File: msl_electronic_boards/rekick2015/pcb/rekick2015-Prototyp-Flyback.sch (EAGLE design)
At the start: 193 parts, among them IC1 LM1458D, IC2 4043D, IC3 LM1117, IC4 LM1458D, Q1 16MHz, Q2 IGW60T120, Q3 IPP023N10N5, Q5 IPD90P04P4L, Q6 IRF840, T2 BC849, T3 BC849, T4 BC849, T5 IRLML6344TRPBF, T6 BC859, U1 TXB0108PWR, U2 SN74LVC2G02DCTR, U3 LM2675, U4 LM2675

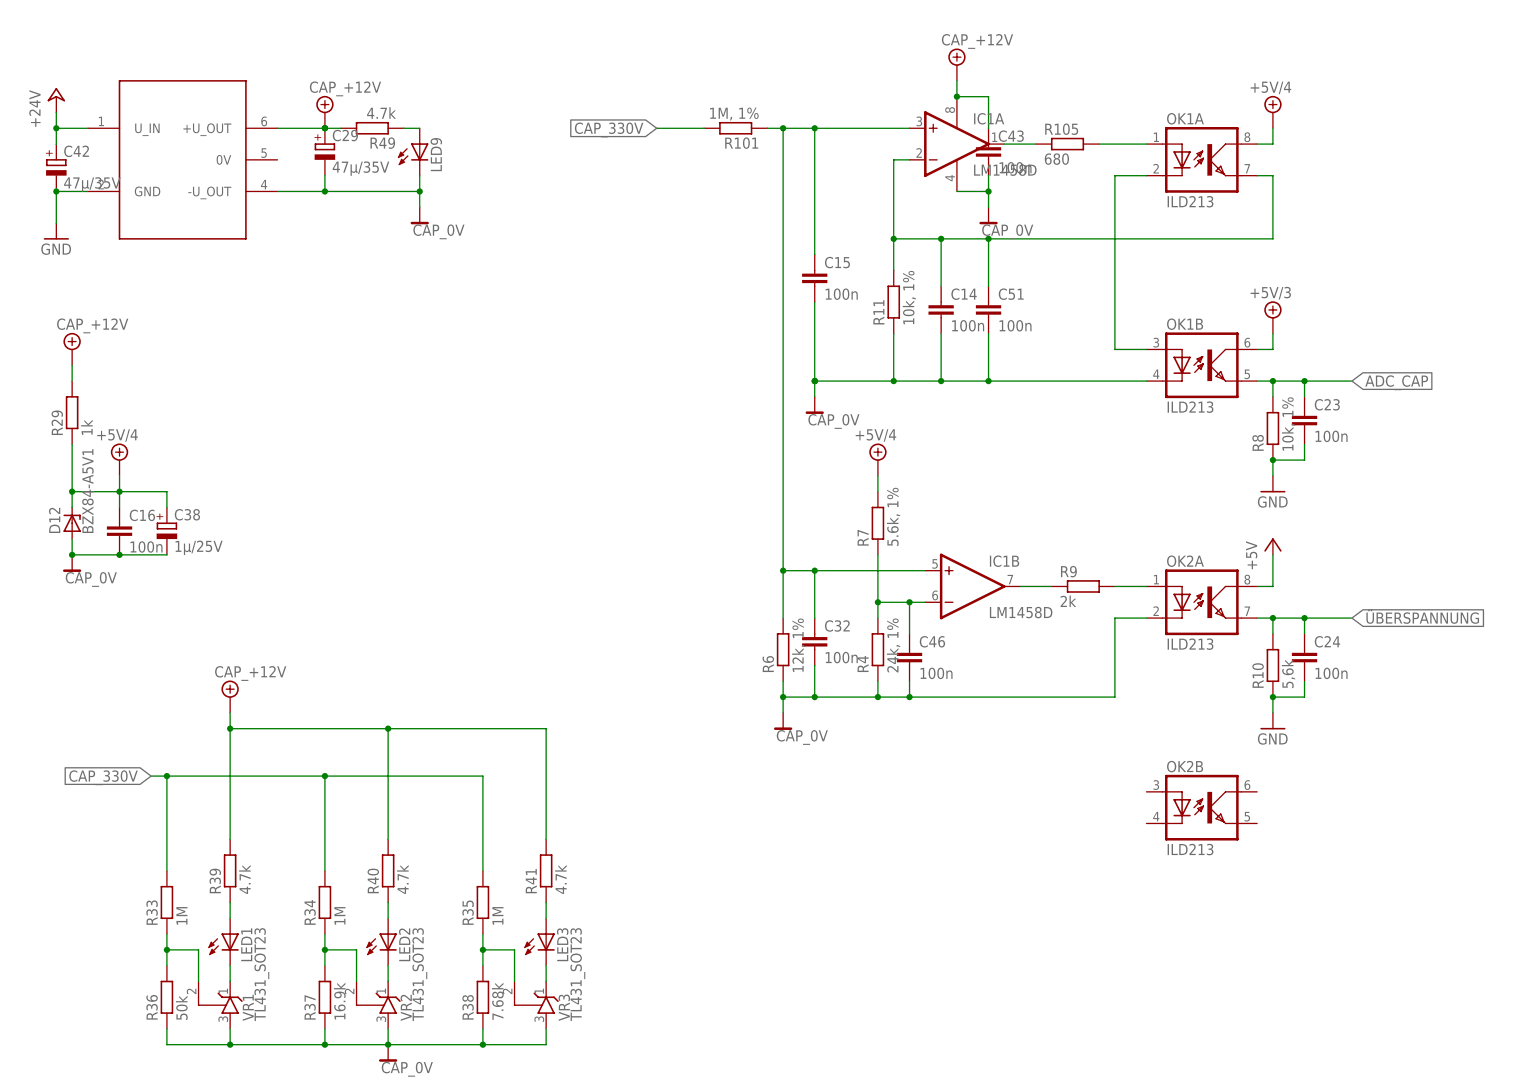
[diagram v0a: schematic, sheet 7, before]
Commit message: rekick flyback
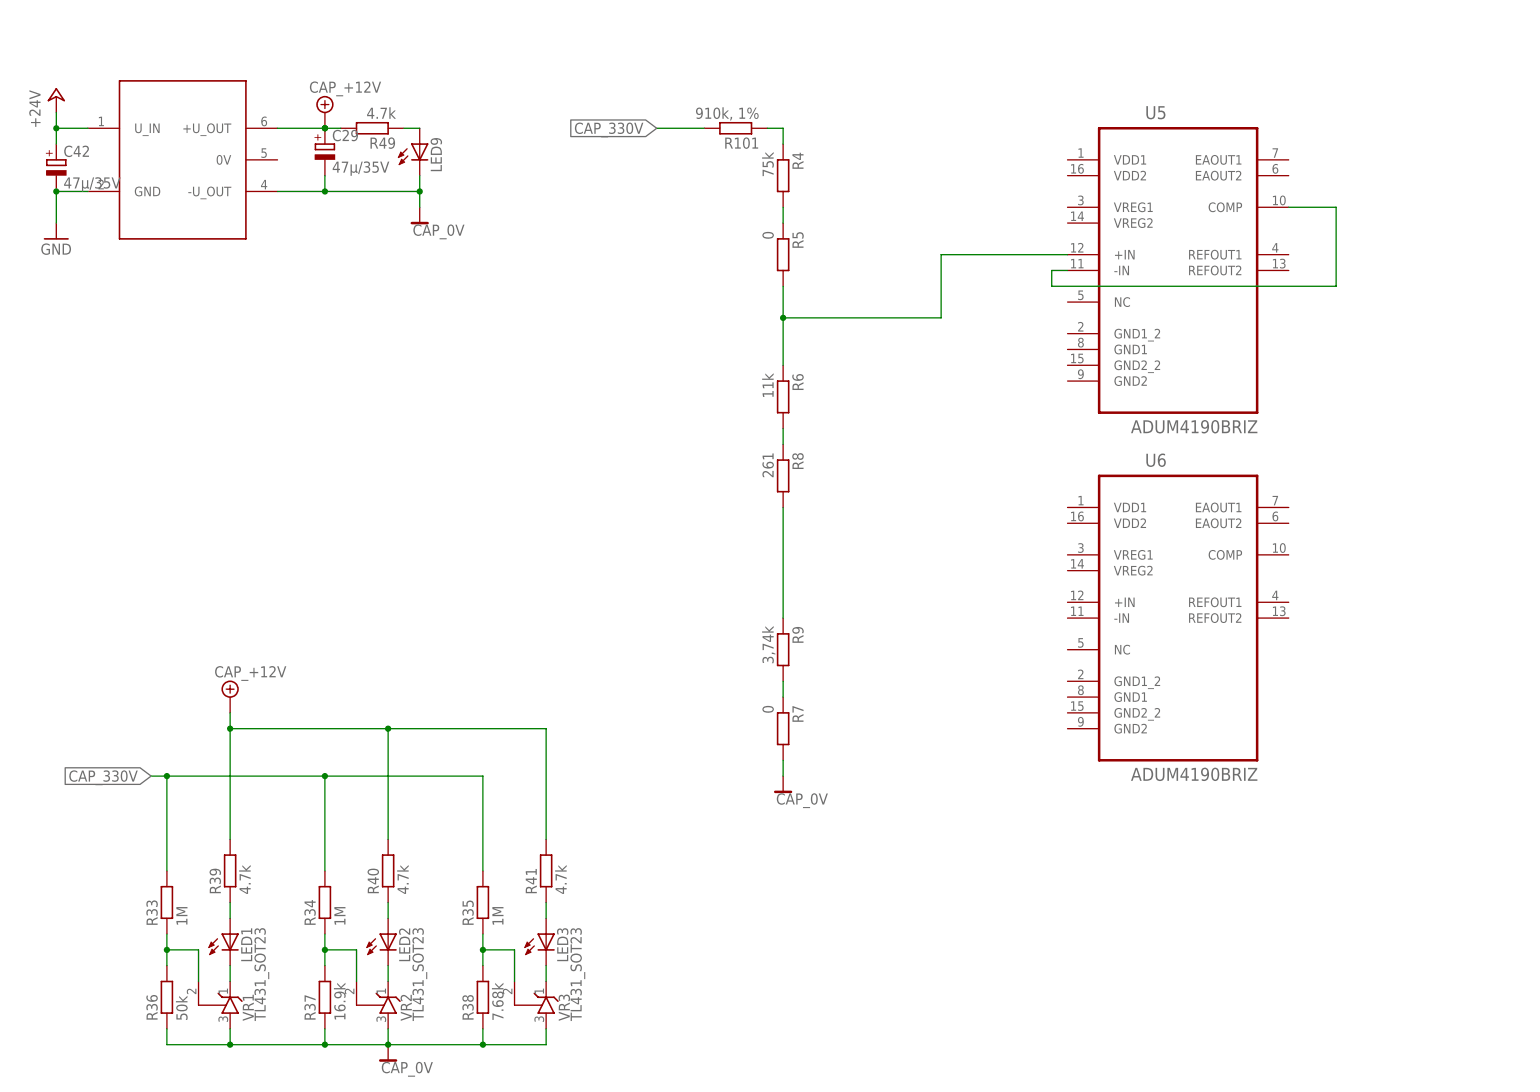
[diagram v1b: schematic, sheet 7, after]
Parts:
- removed C14, C15, C16, C23, C24, C32, C36, C43, C44, C46, C47, C51: 100n, rcl:C-EUC0603
- removed C38: 1µ/25V, rcl:CPOL-EUSMCA
- removed D12: BZX84-A5V1, diode:BZX84CSMD
- removed IC1, IC4: LM1458D, linear:LM1458D
- removed OK1, OK2: ILD213, optocoupler:ILD213
- removed R105: 680, rcl:R-EU_R0805
- removed R12: 10k, rcl:R-EU_R0805
- removed R21: 33k, 1%, rcl:R-EU_R0805
- removed R25: 100k, rcl:R-EU_R0805
- removed R26: 50k, rcl:R-EU_R0805
- removed R29: 1k, rcl:R-EU_R0805
- removed R52: 5,6k, 1%, rcl:R-EU_R0805
- removed T6: BC859, transistor:BC858C-PNP-SOT23-BEC
- added D3: SMD ZD 12, diode:BZX84CSMD
- added R68: 150k, rcl:R-EU_R0805
- added R69, R70, R71: 50k, rcl:R-EU_R0805
- added T1, T7: BC859, transistor:BC858C-PNP-SOT23-BEC
- added U5, U6: ADUM4190BRIZ, adum4190:ADUM4190BRIZ
- R10: value 5,6k -> 910k, 1%; device rcl:R-EU_R0805 -> rcl:R-EU_R2512
- R101: value 1M, 1% -> 910k, 1%
- R11: value 10k, 1% -> 100k
- R13, R18, R66: value 5 -> 4.7
- R4: value 24k, 1% -> 75k
- R48: value 375k -> 220k
- R5: value 10k, 1% -> 0
- R53: value 575k -> 560k
- R54: value 135k -> 130k
- R56: value 375k -> 360k
- R6: value 12k, 1% -> 11k
- R60: value 732 -> 0
- R67: value 375k -> 40.2k
- R7: value 5.6k, 1% -> 0
- R8: value 10k, 1% -> 261
- R9: value 2k -> 3,74k
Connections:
- net N$68 renamed FB
- removed net +5V/4: C16.1, C38.+, D12.C, OK1A.COL, R29.1, R7.2
- removed net CHARGE: U$9.CHARGE
- removed net KICK_VOLTAGE: C36.1, IC4A.-IN, R21.2, R5.1, R52.2
- removed net N$35: OK2A.A, R9.2
- removed net N$50: IC4A.OUT, U2.2B
- removed net N$52: R25.2, T4.B
- removed net N$58: R26.1, T4.C, U2.2A
- new net 0V: R7.2
- new net N$78: R48.1, R68.2, T7.E
- new net N$79: R71.1, T7.B
- new net N$80: R69.1, T1.E, U$9.CHARGE
- new net N$81: R70.1, T1.B
- net +5V: no longer C44.1, IC4P.V+, OK2A.COL, R26.2
- net +5V/3: no longer OK1B.COL, R5.2
- net ACTIVATE_BOOSTER: now also R69.2; no longer R25.1
- net ADC_CAP: no longer C23.1, C47.1, IC4A.+IN, OK1B.EMIT, R8.2
- net CAP_+12V: no longer C43.1, IC1P.V+, R29.2, T6.E
- net CAP_0V: now also D3.A, T4.E; no longer C14.2, C15.2, C16.2, C32.2, C38.-, C43.2, C46.2, C51.2, D12.A, IC1P.V-, OK1B.C, OK2A.C, R12.1, R4.1, R6.1
- net CAP_330V: now also R10.1
- net D2A: no longer R52.1
- net GND: now also T1.C, T7.C; no longer C23.2, C24.2, C36.2, C44.2, C47.2, IC4B.+IN, IC4B.-IN, IC4P.V-, R10.1, R21.1, R8.1, T4.E
- net N$13: now also R7.1, R9.2; no longer IC1A.OUT, R105.1
- net N$14: now also R5.2, R6.1, U5.+IN; no longer C14.1, C51.1, IC1A.-IN, OK1A.EMIT, R11.2
- net N$15: now also R4.2, R5.1; no longer C15.1, C32.1, IC1A.+IN, IC1B.+IN, R101.1, R6.2
- net N$21: now also R101.1, R4.1; no longer OK1A.A, R105.2
- net N$22: now also U5.-IN, U5.COMP; no longer OK1A.C, OK1B.A
- net N$25: now also R8.2; no longer IC1B.OUT
- net N$27: now also R6.2, R8.1; no longer C46.1, IC1B.-IN, R4.2, R7.1
- net N$34: now also R68.1; no longer R48.1
- net N$39: now also D3.C, R10.2, T4.C; no longer R12.2, T6.C
- net N$46: now also R11.2, T4.B; no longer T6.B
- net NOTAUS: now also R70.2, R71.2
- net ÜBERSPANNUNG: no longer C24.1, OK2A.EMIT, R10.2
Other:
- moved on the sheet: C30, R14, R15, R4, R48, R53, R54, R56, R6, R64, R65, R7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

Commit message: rekick flyback
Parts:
- removed LED1: (no value), led:LEDCHIP-LED0805
- removed R3: 100, resistor-power:RHS25
- removed R33, R34: 1M, rcl:R-EU_R2512
- removed R36, R71: 50k, rcl:R-EU_R0805
- removed R37: 16.9k, rcl:R-EU_R0805
- removed R39: 4.7k, rcl:R-EU_R0805
- removed R68: 150k, rcl:R-EU_R0805
- removed R7: 0, rcl:R-EU_R0805
- removed R8: 261, rcl:R-EU_R0805
- removed T7: BC859, transistor:BC858C-PNP-SOT23-BEC
- removed U2: SN74LVC2G02DCTR, SN74LVC2G02DCTR:SN74LVC2G02DCTR
- removed VR1: TL431_SOT23, 1_USER:TL431_SOT23
- added C13, C14, C15, C16, C23, C24, C32, C36: 1µ, rcl:C-EUC0603
- added C38, C43, C49, C57, C58, C59: 100n, rcl:C-EUC0603
- added C44, C46, C47, C48: 10p, rcl:C-EUC0603
- added C51: 10µ/50V, rcl:C-EUC1206
- added C52, C53, C54, C55, C56: (no value), rcl:CPOL-EUE2.5-7
- added D4, D8: BZX84-A5V1, diode:BZX84CSMD
- added IC1: 74LVC1G02GW, 74xx-little-de:74AHC1G02DBV
- added IC4: LM1458D, linear:LM1458D
- added KK1, KK2, KK3: SK104, heatsink:SK104
- added LED11: (no value), led:LEDCHIPLED_0603
- added Q4: PSMN7R8-120PS, transistor-power:PMOSFET_NTO220BV
- added R12, R21, R25: 1k, rcl:R-EU_R0805
- added R26, R29: 100k, rcl:R-EU_R0805
- added R52, R72: 10k, rcl:R-EU_R0805
- added R73: 10m, R2818:R2818
- added R74: 2, R2818:R2818
- added U$10, U$11: RTO50, RTO50:RTO50
- C10, C9: value 2200µ/50V -> 10µ/50V; device rcl:CPOL-EUE5-13 -> rcl:C-EUC1206
- C11: device rcl:C-EUC1206 -> rcl:C-EUC2220K
- C12: value 100n -> 10µ/50V; device rcl:C-EUC0603 -> rcl:C-EUC1206
- C30, C31: device rcl:CPOL-EUE2-5 -> rcl:C-EUC1206
- C35, C50: value 1µ/50V -> 10µ/50V
- C41: value 100n -> 22n; device rcl:C-EUC0603 -> rcl:C-EUC1206
- D9: value STTH1R06A -> STTH810D; device diode:GF1 -> diode:BYT08P
- Q3: value IPP023N10N5 -> PSMN7R8-120PS
- R10, R101: value 910k, 1% -> 1M, 1%; device rcl:R-EU_R2512 -> rcl:R-EU_R1206
- R13, R18: device rcl:R-EU_R2512 -> rcl:R-EU_R0805
- R2: value 100 -> 1M, 1%; device resistor-power:RHS25 -> rcl:R-EU_R1206
- R35: value 1M -> 4.7k; device rcl:R-EU_R2512 -> rcl:R-EU_R0805
- R38: value 7.68k -> 5.6k
- R4: value 75k -> 140k
- R40, R41: value 4.7k -> 1k
- R43, R45: value 1,5k -> 1k
- R57: value 5,6k -> 3.2k
- R6: value 11k -> 12.4k
- R63: value 6m -> 10m; device rcl:R-EU_R0805 -> R2818:R2818
- R9: value 3,74k -> 4,7k
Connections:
- removed net 0V: R7.2
- removed net ADC9/FREI: U$2.PC5
- removed net ADC_24V_PRI: U$2.PD5
- removed net D2A: U$2.PC7
- removed net FREI: U$2.PB2
- removed net FREI2: U$2.PB6
- removed net N$12: R33.1, R36.2, VR1.R
- removed net N$13: R7.1, R9.2
- removed net N$2: LED1.C, VR1.C
- removed net N$25: R8.2, R9.1
- removed net N$34: R68.1, U$9.UVLO1
- removed net N$60: R34.1, R37.2, VR2.R
- removed net N$64: LED1.A, R39.1
- removed net N$79: R71.1, T7.B
- removed net N$80: R69.1, T1.E, U$9.CHARGE
- removed net STBY: R57.2, U2.2Y
- new net !CHARGE: R69.1, T1.E, U$2.PC4, U$9.CHARGE
- new net ADC_CAP_OV: IC4A.+IN, R52.1, U5.EAOUT1
- new net N$35: R12.1, S1.P, S1.P1
- new net N$50: C15.1, U5.VREG1
- new net N$52: C16.1, U5.VREG2
- new net N$58: C36.1, U6.VREG2
- new net N$68: C32.1, U6.VREG1
- new net N$82: R21.2, R26.2, U6.+IN
- new net N$83: R29.1, U6.COMP
- new net N$84: C47.1, R25.1, U6.REFOUT2
- new net N$85: R25.2, R29.2, U6.-IN
- new net N$86: C41.2, R74.1
- new net N$89: C44.1, U5.REFOUT2
- new net N$90: C46.1, U5.REFOUT1
- new net N$91: R72.1, U6.EAOUT1
- new net N$93: C48.1, U6.REFOUT1
- net !FAULT: now also U$2.PC5
- net +12V: now also C13.1, C23.1, U5.VDD1, U6.VDD1
- net +5V: now also C49.1, IC1P.VCC, IC4P.V+, R12.2, R40.2, R41.2, R57.1; no longer S1.S, S1.S1, U2.VCC
- net +5V/3: now also IC4A.-IN
- net ADC_24V_BOOSTER: now also C58.2, U$2.PD5
- net ADC_24V_LOGIK/SCK_A: now also C59.2
- net ADC_CAP: now also C57.1, D8.C, R35.2, R52.2, VR2.R
- net CAP_+12V: now also C14.1, C24.1, C30.1, C31.1, U5.VDD2, U6.VDD2; no longer C30.+, C31.+, R39.2, R40.2, R41.2
- net CAP_0V: now also C14.2, C16.2, C24.2, C30.2, C31.2, C36.2, C38.2, C43.2, C44.2, C47.2, R26.1, R9.2, U5.GND2, U5.GND2_2, U6.GND2, U6.GND2_2; no longer C30.-, C31.-, R36.1, R37.1, VR1.A
- net CAP_330V: now also U$10.1; no longer R33.2, R34.2, R35.2
- net CLKOUT_ETH: now also U1.B6; no longer U1.B8
- net CLKOUT_ETH_3V: now also U1.A6; no longer U1.A8
- net FB: now also D4.C, R72.2
- net GND: now also C13.2, C15.2, C23.2, C32.2, C46.2, C48.2, C49.2, C57.2, C58.1, C59.1, D4.A, D8.A, IC1P.GND, IC4P.V-, U5.GND1, U5.GND1_2, U5.NC, U6.GND1, U6.GND1_2, U6.NC; no longer C41.2, T7.C, U2.GND
- net GND1: now also C10.2, C51.2, C52.-, C53.-, C54.-, C55.-, C56.-, C9.2, R73.2; no longer C10.-, C9.-
- net N$14: now also C43.1
- net N$16: now also Q4.D, R74.2
- net N$17: now also Q4.S, R73.1
- net N$18: now also Q4.G
- net N$23: now also U$10.2, U$11.1; no longer R2.2, R3.1
- net N$24: now also U$11.2; no longer R3.2
- net N$27: now also C38.1, R21.1, R9.1; no longer R8.1
- net N$37: now also IC1A.I0; no longer U2.1A
- net N$38: now also IC1A.I1; no longer U2.1B
- net N$39: now also R2.2
- net N$59: now also R48.1, U$9.UVLO1; no longer R57.1, U$2.PC4
- net N$78: now also LED11.A, R57.2; no longer R48.1, R68.2, T7.E
- net N$8: now also C10.1, C41.1, C51.1, C52.+, C53.+, C54.+, C55.+, C56.+, C9.1; no longer C10.+, C9.+
- net NOTAUS: now also IC1A.O, LED11.C; no longer R71.2, U2.1Y
- net RST_ETH: now also U1.B8; no longer U1.B6
- net RST_ETH_3V: now also U1.A8; no longer U1.A6
- net TASTER: now also S1.S, S1.S1; no longer S1.P, S1.P1
- net ÜBERSPANNUNG: now also IC4A.OUT; no longer C41.1
